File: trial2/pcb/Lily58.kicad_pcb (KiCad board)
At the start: 2 copper layers, 142.5 x 106.3 mm, 120 parts, among them J1 LED, J2 4PIN, P1 i2c_pin, P2 i2c_pin, P3 ICSP, P4 OLED, SW1 SW_PUSH, SW10 SW_PUSH, SW11 SW_PUSH, SW12 SW_PUSH, SW13 SW_PUSH, SW14 SW_PUSH, SW15 SW_PUSH, SW16 SW_PUSH, SW17 SW_PUSH, SW18 SW_PUSH, SW19 SW_PUSH, SW2 SW_PUSH, SW20 SW_PUSH, SW21 SW_PUSH, SW22 SW_PUSH, SW23 SW_PUSH, SW24 SW_PUSH, SW25 Rotary_Encoder_Switch, SW26 SW_PUSH, SW27 SW_PUSH, SW28 SW_PUSH, SW29 SW_PUSH, SW3 SW_PUSH, SW4 SW_PUSH, SW5 SW_PUSH, SW6 SW_PUSH, SW7 SW_PUSH, SW8 SW_PUSH, SW9 SW_PUSH, U1 ProMicro

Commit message: Working on Vias
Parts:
- removed J2: 4PIN, Lily58-footprint:MJ-4PP-9
- removed P1, P2: i2c_pin, Lily58-footprint:1pin_conn
- removed P3: ICSP, Lily58-footprint:ICSP
- removed R1, R2: R, Lily58-footprint:RESISTOR_mini
- removed W1: jumper, Lily58-footprint:jumper_data
- added LEDVCC1: SW_DIP_x02, Package_DIP:DIP-4_W7.62mm, F.Cu at (85.1, 89.5)
- SW1, SW10, SW11, SW12, SW13, SW14, SW15, SW16, SW17, SW18, SW19, SW2, SW20, SW21, SW22, SW23, SW24, SW27, SW28, SW29, SW3, SW4, SW5, SW6, SW7, SW8, SW9: footprint Lily58-footprint:MX_PG1350_FLIP_HOLES_18mm -> Lily58-footprint:MX_Socket_18mm
- SW26: footprint Lily58-footprint:MX_PG1350_FLIP_HOLES_27mm -> Lily58-footprint:MX_Socket_18mm
- U1: value ProMicro -> NiceNano
- moved D4 66.4 mm to (151.3, 111.7), turned to 0 degrees
- moved RSW1 26.0 mm to (85.7, 42.5), turned to 90 degrees
- moved D25 2.85 mm to (100.3, 78.1)
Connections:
- net Net-(U1-Pad24) renamed Batt+
- L1 pad 3: Net-(L1-Pad3) -> LEDunder
- L1 pad 4: VCC -> Net-(L1-Pad4)
- L2 pad 4: VCC -> Net-(L1-Pad4)
- L3 pad 4: VCC -> Net-(L1-Pad4)
- L30 pad 1: Net-(L30-Pad1) -> unconnected-(L30-Pad1)
- L31 pad 1: Net-(L1-Pad3) -> LEDback
- L31 pad 4: VCC -> Net-(L31-Pad4)
- L32 pad 4: VCC -> Net-(L31-Pad4)
- L33 pad 4: VCC -> Net-(L31-Pad4)
- L4 pad 4: VCC -> Net-(L1-Pad4)
- L5 pad 4: VCC -> Net-(L1-Pad4)
- L6 pad 4: VCC -> Net-(L1-Pad4)
- U1 pad 1: LED -> LEDunder
- U1 pad 2: DATA -> LEDback
- U1 pad 20: Net-(U1-Pad20) -> unconnected-(U1-Pad20)
- U1 pad 23: GND -> Batt-
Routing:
- net VCC: track 1045.9 -> 70.6 mm, vias 44 -> 0
- net SDA: track 53.7 -> 777.7 mm, vias 3 -> 53
- net col2: track 314.4 -> 14.6 mm, vias 1 -> 2
- net col3: track 300.2 -> 15.7 mm, vias 1 -> 2
- net col4: track 291.3 -> 15.1 mm, vias 0 -> 2
- net col1: track 382.1 -> 114.5 mm
- net col0: track 270.9 -> 15.1 mm, vias 0 -> 3
- net row4: track 176.0 -> 15.3 mm, vias 5 -> 0
- net col5: track 185.4 -> 29.1 mm, vias 2 -> 0
- net row1: track 148.7 -> 17.0 mm, vias 7 -> 0
- net GND: track 1095.1 -> 982.2 mm, vias 73 -> 42
- net Net-(L27-Pad1): track 64.0 -> 0.00 mm, vias 3 -> 0
- net DATA: track 60.9 -> 0.00 mm, vias 3 -> 0
- net row3: track 181.9 -> 124.4 mm, vias 6 -> 5
- net LED: track 121.3 -> 68.5 mm, vias 5 -> 4
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- added copper zone on B.Cu, net SDA
- added copper zone on F.Cu, net SDA
- removed copper zone on B.Cu, net GND
- removed copper zone on F.Cu, net GND
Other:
- net class Default removed
- net class GND removed
- net class VCC removed
- board text added: "Lily58-Glow-Enc-Wireless-v1.0"
- board text added: "kata0510/Lily58 => qtkb/Lily58-Glow => orvisevans/Lily58-Glow-Enc => iasoren/Lily58-Glow-Enc-Wireless"
- board text removed: "Lily58-Glow-Enc-v1.0"
- board text removed: "kata0510/Lily58 => qtkb/Lily58-Glow => orvisevans/Lily58-Glow-Enc"

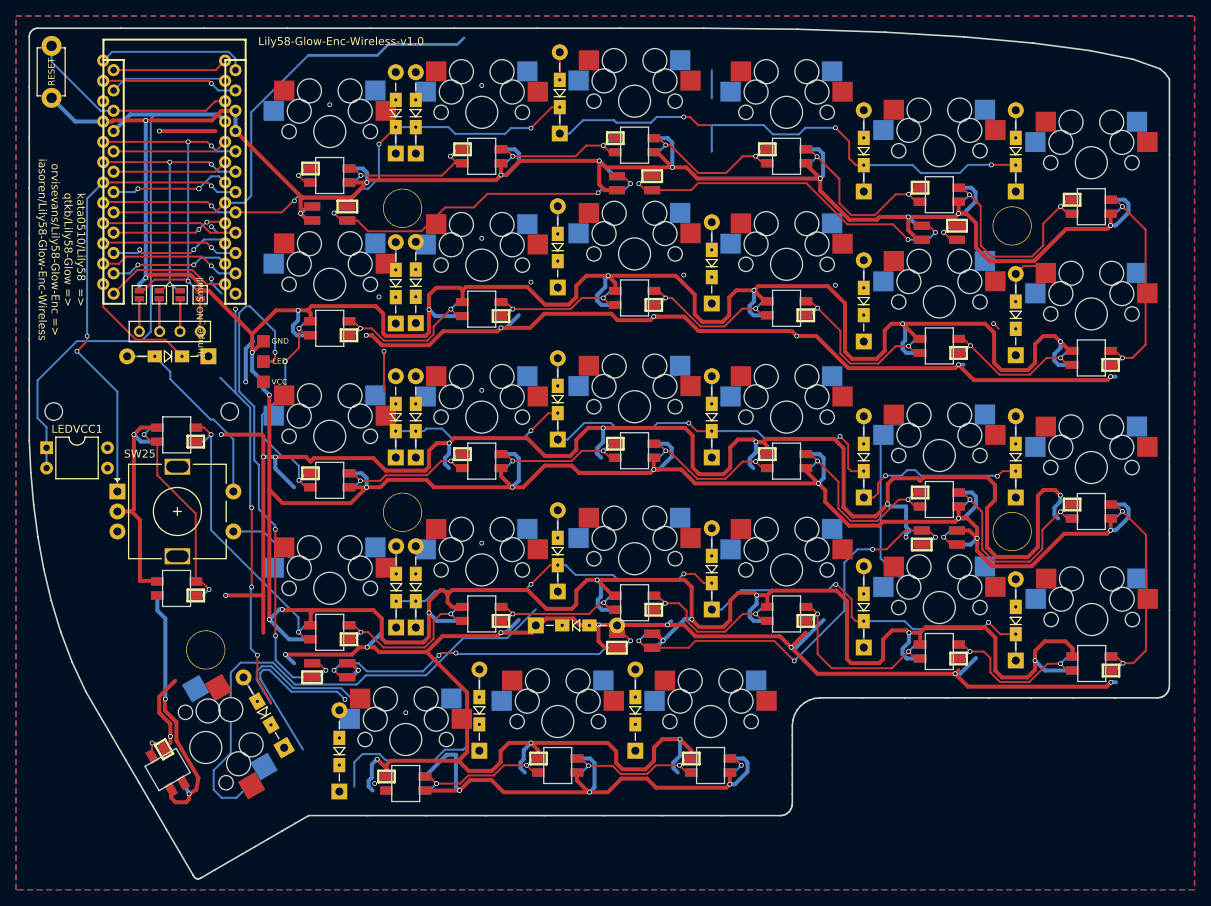
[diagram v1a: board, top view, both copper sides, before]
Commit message: Add libraries, new design
Turns out DIP switches aren't rated for the LED current, so I need a SPDT switch with a diode placed in between. This means you can have the backlight on, none on, or the backlight and underglow on. I might reverse this decision later on. Who knows
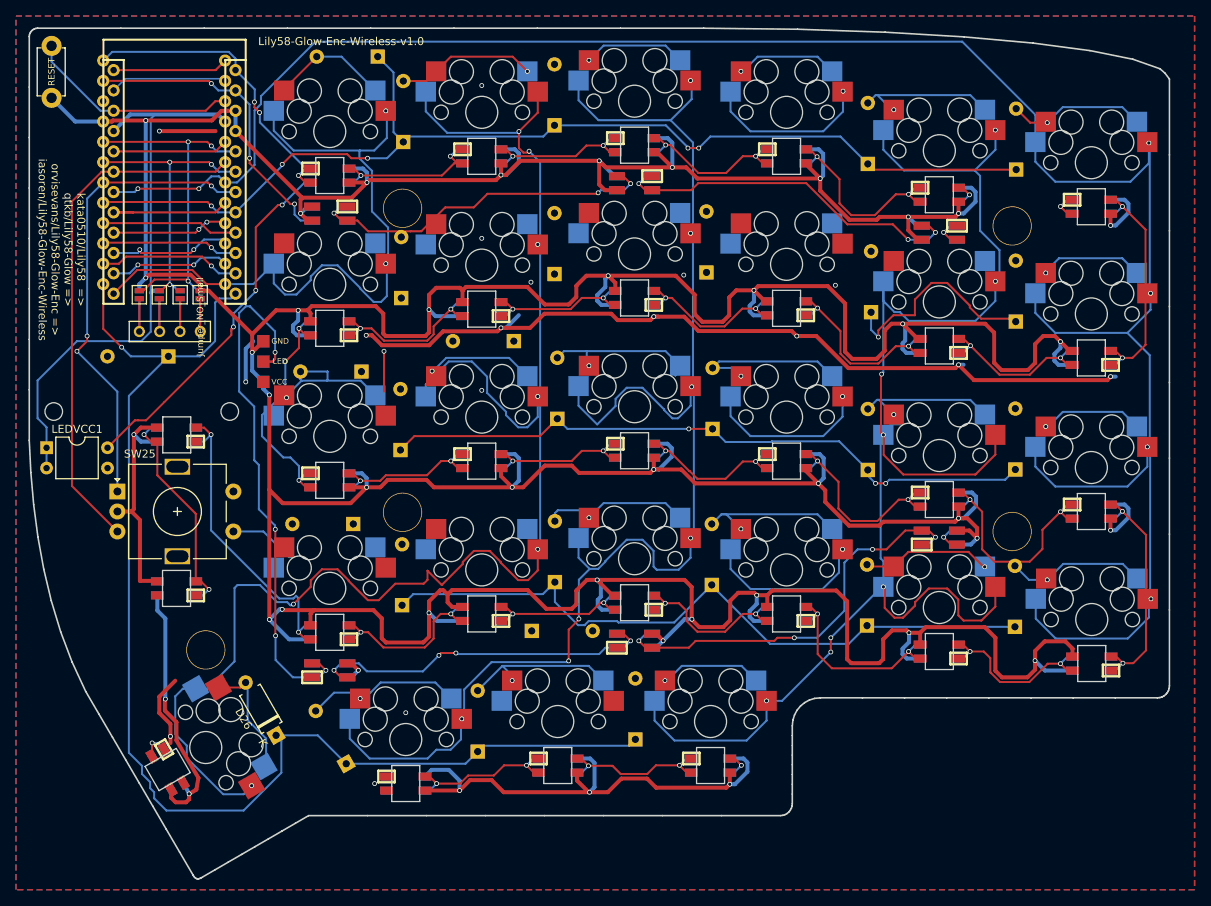
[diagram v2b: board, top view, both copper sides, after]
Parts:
- D1, D10, D11, D12, D13, D14, D15, D16, D17, D18, D19, D2, D20, D21, D22, D23, D24, D25, D26, D27, D28, D29, D3, D4, D5, D6, D7, D8, D9: footprint Lily58-footprint:Diode_TH_SOD123 -> Diode_THT:D_A-405_P7.62mm_Horizontal
- moved D8 14.2 mm to (143.5, 76.2), turned to 180 degrees
- moved D19 9.58 mm to (123.4, 99.1), turned to 180 degrees
- moved D1 7.46 mm to (126.5, 40.6), turned to 180 degrees
- moved D13 7.17 mm to (124.5, 80.0), turned to 180 degrees
- moved D4 5.55 mm to (145.7, 112.4)
- moved D28 5.11 mm to (139.0, 127.5)
- moved D14 4.49 mm to (129.3, 89.8)
- moved D3 4.03 mm to (148.6, 49.2)
- moved D2 3.88 mm to (129.7, 51.3)
- moved D21 3.84 mm to (148.6, 106.3)
- moved D29 3.58 mm to (158.7, 126.0)
- moved D9 3.34 mm to (148.6, 67.8)
- moved D26 3.15 mm to (113.8, 125.5)
- moved D20 2.80 mm to (129.5, 109.2)
- moved D15 2.40 mm to (148.9, 85.9)
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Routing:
- net SDA: track 777.7 -> 174.7 mm, vias 53 -> 21
- net col0: track 15.1 -> 273.6 mm, vias 3 -> 6
- net col4: track 15.1 -> 205.7 mm, vias 2 -> 9
- net col3: track 15.7 -> 191.9 mm, vias 2 -> 9
- net row4: track 15.3 -> 158.5 mm, vias 0 -> 1
- net col1: track 114.5 -> 212.8 mm, vias 0 -> 8
- net col5: track 29.1 -> 99.1 mm, vias 0 -> 2
- net col2: track 14.6 -> 77.7 mm, vias 2 -> 5
- net GND: track 982.2 -> 926.4 mm
- net enc2: track 14.4 -> 64.8 mm
- net Net-(L1-Pad4): track 0.00 -> 45.3 mm, vias 0 -> 3
- net row1: track 17.0 -> 44.3 mm, vias 0 -> 1
- net row2: track 124.9 -> 100.3 mm, vias 6 -> 4
- net Net-(D25-Pad2): track 24.6 -> 0.00 mm
- net Net-(L5-Pad1): track 28.8 -> 4.95 mm
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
